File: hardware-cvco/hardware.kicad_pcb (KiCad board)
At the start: 4 copper layers, 99 x 75 mm, 167 parts, among them J1 SMA, J2 SMA, J3 SMA, J4 SMA, J5 SMA, J6 SMA, J7 SMA, J8 Pickit 2, J9 DC, Q1 AOD403, Q2 MBT2222, SW1 On/Off, U1 74LS07, U10 TPS61046, U11 BQ21040, U12 LM324, U13 LM317DCYR, U14 LM386, U2 NLB-310-T1, U3 NLB-310-T1, U4 NLB-310-T1, U5 NLB-310-T1, U6 PIC12F675-ISN, U7 NLB-310-T1, U8 NLB-310-T1, U9 NLB-310-T1, Y1 CVCO55CW-0100-0200, Y2 CVCO55CW-0200-0500, Y3 CV55CW500-1000, Y4 CVCO55CW-1000-2000, Y5 CV55BE1600-3200, Y6 CVCO55CC-3180-3710, Y7 CVCO55CW-3500-4500

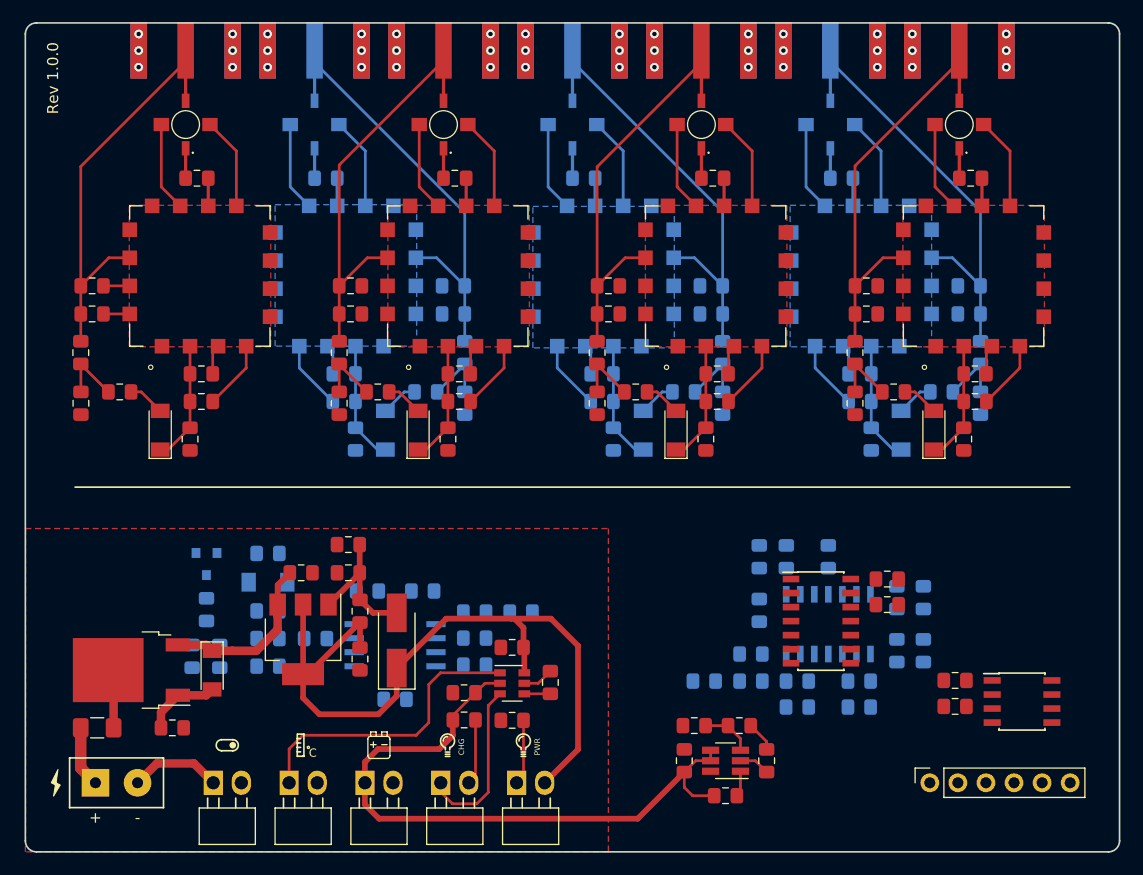
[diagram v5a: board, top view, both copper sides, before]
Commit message: Sweep Generator routing - CVCO.
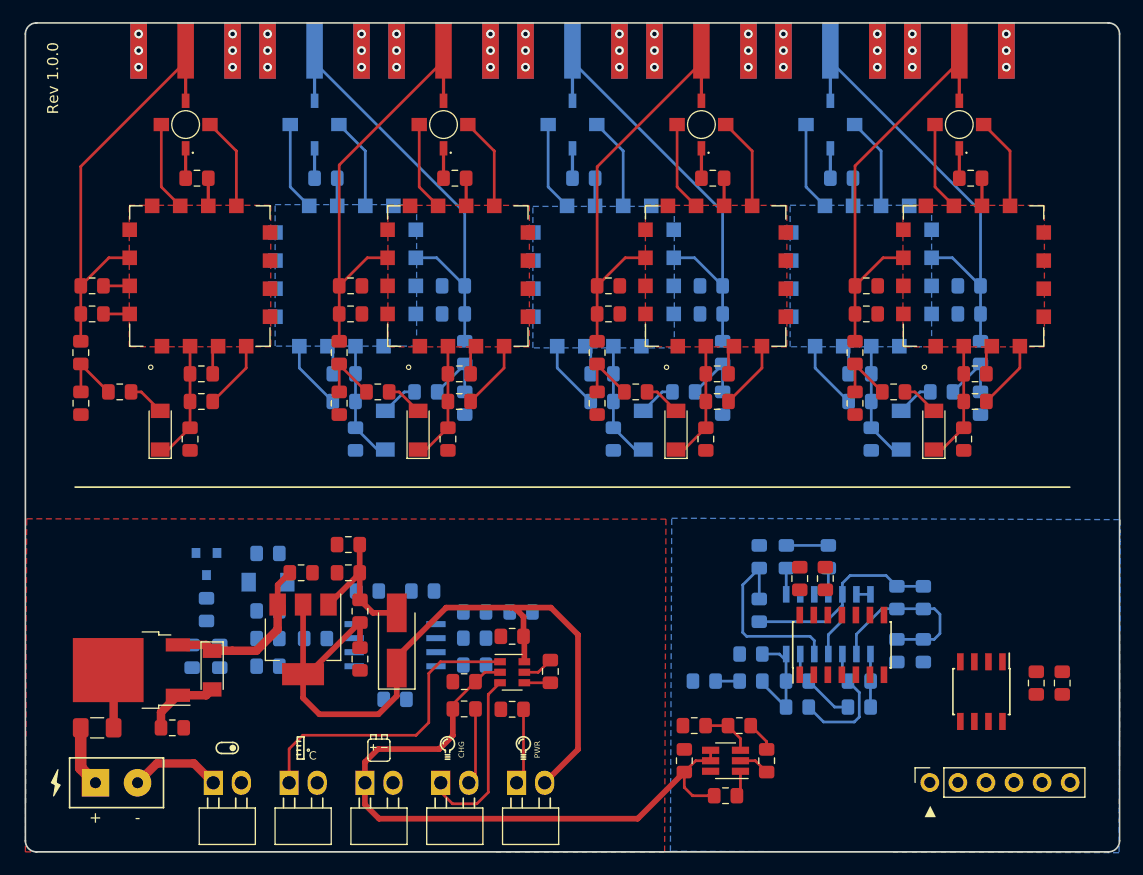
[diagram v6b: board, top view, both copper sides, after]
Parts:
- moved C25 9.92 mm to (159.3, 111.7), turned to 90 degrees
- moved C24 7.92 mm to (135.6, 102.3), turned to 270 degrees
- moved C26 7.35 mm to (157.0, 111.7), turned to 90 degrees
- moved C23 6.08 mm to (137.9, 102.3), turned to 270 degrees
- moved U6 3.78 mm to (152.0, 112.5), turned to 270 degrees
- moved U1 2.87 mm to (139.4, 108.3), turned to 90 degrees
- moved C45 1.00 mm to (105.2, 111.6)
- moved C46 1.00 mm to (109.5, 107.5)
- moved R33 1.00 mm to (105.2, 114.1)
- moved R34 1.00 mm to (113.0, 110.7)
- moved R36 1.00 mm to (109.5, 114.1)
- moved U11 1.00 mm to (109.5, 110.8)
- moved G*** 0.25 mm to (110.6, 117.6)
- moved G*** 0.25 mm to (103.7, 117.6)
- moved G*** 0.25 mm to (90.4, 117.6)
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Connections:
- C23 pad 2: Net-(C23-Pad2) -> P2_VSS
- C24 pad 2: Net-(C23-Pad2) -> P2_VSS
- C25 pad 2: Net-(C25-Pad2) -> P2_VSS
- C26 pad 2: Net-(C25-Pad2) -> P2_VSS
- J8 pad 4: Net-(J8-Pad4) -> GP1
- J8 pad 5: GP1 -> GP0
- J8 pad 6: GP0 -> Net-(J8-Pad6)
- U1 pad 14: Net-(C23-Pad2) -> P2_VDD
- U12 pad 5: Net-(C44-Pad2) -> Net-(R51-Pad1)
- U12 pad 6: Net-(R51-Pad1) -> Net-(C44-Pad2)
- U6 pad 1: Net-(C25-Pad2) -> P2_VDD
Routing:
- net P2_VDD: track 2.75 -> 25.8 mm
- net Net-(R51-Pad1): track 0.00 -> 17.2 mm
- net VGND: track 0.00 -> 16.4 mm
- net Net-(R41-Pad2): track 0.00 -> 11.7 mm
- net Sweep: track 0.00 -> 9.83 mm
- net Net-(C44-Pad2): track 0.00 -> 7.29 mm
- net Net-(R37-Pad2): track 0.00 -> 4.81 mm
- net Net-(R53-Pad2): track 0.00 -> 3.80 mm
- net Tuner: track 0.00 -> 2.38 mm
- net P2_VSS: track 211.3 -> 213.7 mm
- net Net-(C13-Pad1): track 0.00 -> 2.17 mm
- net DC: track 69.2 -> 71.2 mm
- net Net-(U12-Pad13): track 0.00 -> 1.27 mm
- net Net-(D9-Pad2): track 5.93 -> 6.94 mm
- net Net-(TH1-Pad1): track 27.0 -> 28.0 mm
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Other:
- board text added: "▸"

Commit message: Noise Source routing - CVCO.
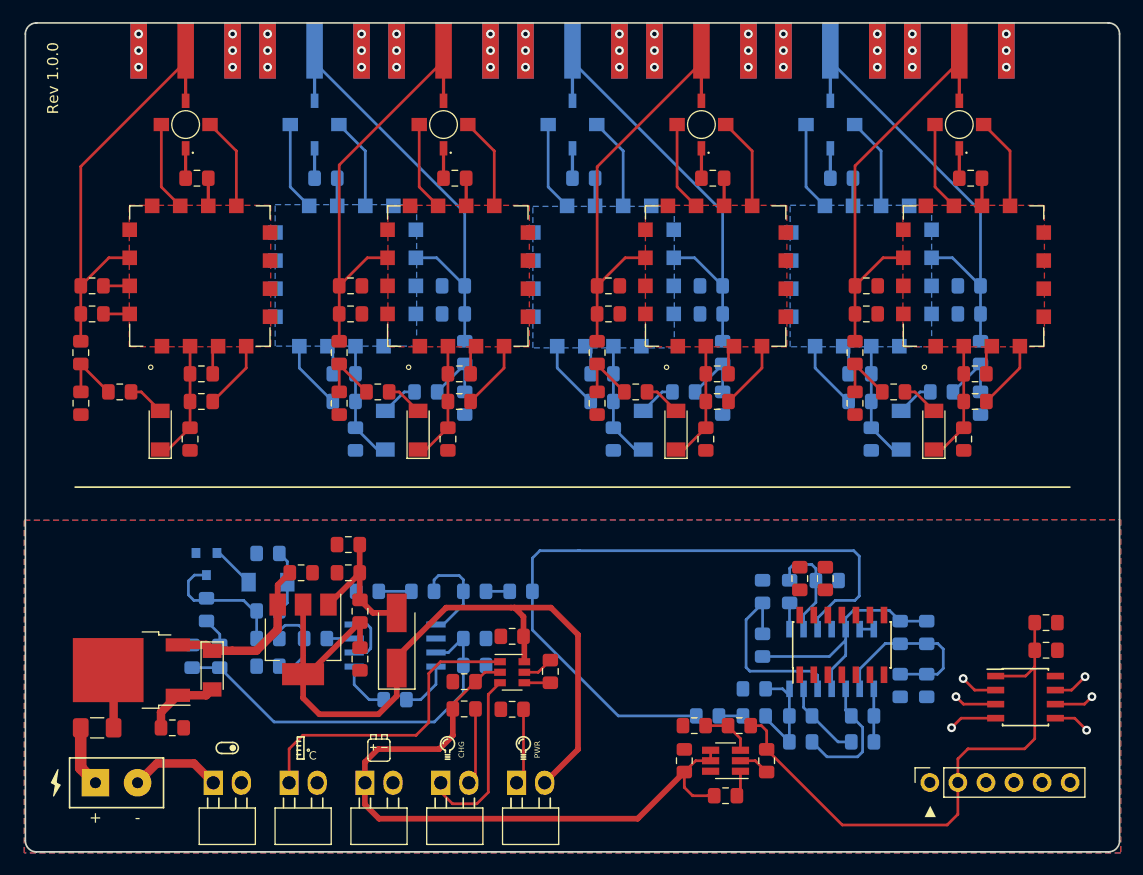
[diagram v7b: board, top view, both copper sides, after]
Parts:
- C47: value 0.1μF -> 1μF
- moved C25 5.66 mm to (157.8, 106.3), turned to 0 degrees
- moved U6 4.02 mm to (156.0, 113.0), turned to 0 degrees
- moved C44 3.16 mm to (135.7, 114.7)
- moved C49 3.16 mm to (144.7, 107.2)
- moved C53 3.16 mm to (144.7, 112.0)
- moved R38 3.16 mm to (147.1, 107.2)
- moved R41 3.16 mm to (141.2, 114.7)
- moved R46 3.16 mm to (147.1, 112.0)
- moved R53 3.16 mm to (134.7, 103.5)
- moved R17 3.16 mm to (127.2, 114.7)
- moved C13 3.16 mm to (131.4, 114.7)
- moved R43 3.16 mm to (131.4, 112.2)
- moved R52 3.16 mm to (132.2, 103.5)
- moved R37 3.16 mm to (141.2, 117.0)
- moved R47 3.16 mm to (135.7, 117.0)
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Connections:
- C47 pad 1: Net-(C47-Pad1) -> P2_VSS
- C48 pad 1: Net-(C47-Pad1) -> P2_VSS
- C56 pad 2: Net-(C50-Pad2) -> Net-(C50-Pad1)
- R45 pad 1: Net-(C50-Pad2) -> Net-(C50-Pad1)
- U14 pad 3: Net-(C50-Pad1) -> Net-(C50-Pad2)
- U14 pad 6: Net-(C47-Pad1) -> Net-(U14-Pad6)
- U14 pad 7: Net-(U14-Pad7) -> Net-(C47-Pad2)
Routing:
- net Net-(R17-Pad1): track 0.00 -> 63.9 mm
- net P2_VDD: track 25.8 -> 76.7 mm
- net Net-(C47-Pad2): track 0.00 -> 35.6 mm
- net GP1: track 0.00 -> 22.6 mm, vias 0 -> 1
- net GP0: track 0.00 -> 15.8 mm, vias 0 -> 1
- net Net-(Q2-Pad3): track 0.00 -> 12.3 mm
- net GP3: track 0.00 -> 10.1 mm, vias 0 -> 1
- net Noise: track 0.00 -> 9.72 mm
- net Net-(C50-Pad1): track 0.00 -> 8.27 mm
- net Net-(R53-Pad2): track 3.80 -> 9.69 mm
- net Net-(C55-Pad2): track 0.00 -> 5.80 mm
- net Net-(C58-Pad2): track 0.00 -> 4.88 mm
- net Net-(C58-Pad1): track 0.00 -> 4.86 mm
- net Net-(D12-Pad2): track 0.00 -> 3.96 mm
- net GP4: track 0.00 -> 3.87 mm, vias 0 -> 1
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
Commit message: PIC routing - CVCO.
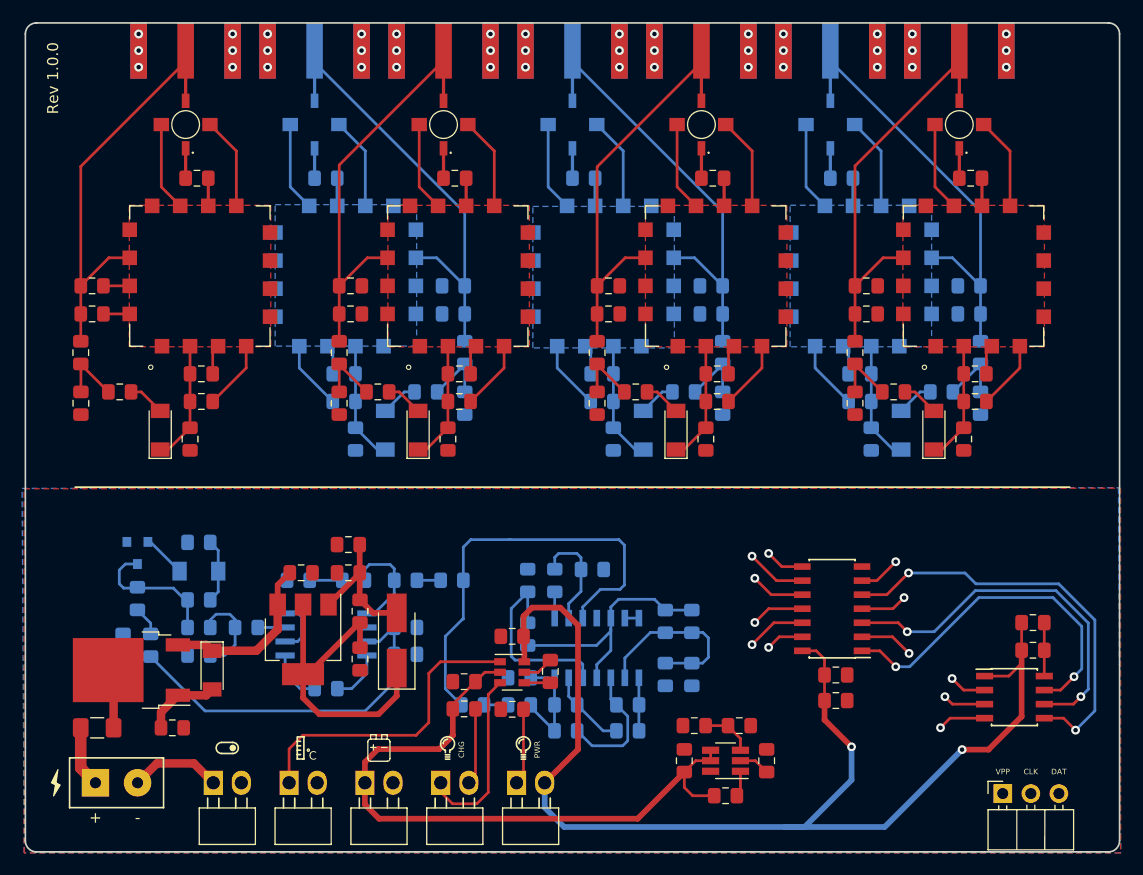
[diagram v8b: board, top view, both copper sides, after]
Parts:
- J8: footprint Connector_PinSocket_2.54mm:PinSocket_1x06_P2.54mm_Vertical -> Connector_PinSocket_2.54mm:PinSocket_1x03_P2.54mm_Horizontal
- moved R38 21.3 mm to (125.8, 106.2)
- moved R46 21.3 mm to (125.8, 111.0)
- moved R54 21.3 mm to (116.8, 101.5)
- moved C44 21.3 mm to (114.4, 113.7)
- moved C49 21.3 mm to (123.4, 106.2)
- moved C53 21.3 mm to (123.4, 111.0)
- moved R17 21.3 mm to (106.0, 113.7)
- moved R37 21.3 mm to (120.0, 116.0)
- moved R41 21.3 mm to (120.0, 113.7)
- moved R47 21.3 mm to (114.4, 116.0)
- moved R53 21.3 mm to (113.4, 102.5)
- moved C13 21.3 mm to (110.2, 113.7)
- moved R43 21.3 mm to (110.2, 111.2)
- moved R51 21.3 mm to (111.0, 107.3)
- moved R52 21.3 mm to (111.0, 102.5)
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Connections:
- BT1 pad 2: P2_VSS -> GND
- C1 pad 2: P2_VSS -> GND
- C14 pad 2: P2_VSS -> GND
- C15 pad 2: P2_VSS -> GND
- C16 pad 2: P2_VSS -> GND
- C17 pad 2: P2_VSS -> GND
- C18 pad 2: P2_VSS -> GND
- C19 pad 2: P2_VSS -> GND
- C2 pad 2: P2_VSS -> GND
- C20 pad 2: P2_VSS -> GND
- C21 pad 2: P2_VSS -> GND
- C23 pad 1: P2_VDD -> VDD
- C23 pad 2: P2_VSS -> GND
- C24 pad 1: P2_VDD -> VDD
- C24 pad 2: P2_VSS -> GND
- C25 pad 1: P2_VDD -> VDD
- C25 pad 2: P2_VSS -> GND
- C26 pad 1: P2_VDD -> VDD
- C26 pad 2: P2_VSS -> GND
- C27 pad 2: P2_VSS -> GND
- C28 pad 2: P2_VSS -> GND
- C29 pad 2: P2_VSS -> GND
- C3 pad 2: P2_VSS -> GND
- C30 pad 2: P2_VSS -> GND
- C31 pad 2: P2_VSS -> GND
- C32 pad 2: P2_VSS -> GND
- C36 pad 1: P2_VDD -> Boost
- C36 pad 2: P2_VSS -> GND
- C37 pad 2: P2_VSS -> GND
- C38 pad 2: P2_VSS -> GND
- C39 pad 2: P2_VSS -> GND
- C4 pad 2: P2_VSS -> GND
- C40 pad 2: P2_VSS -> GND
- C41 pad 2: P2_VSS -> GND
- C42 pad 2: P2_VSS -> GND
- C43 pad 2: P2_VSS -> GND
- C45 pad 2: P2_VSS -> GND
- C46 pad 1: DC -> VDD
- C46 pad 2: P2_VSS -> GND
- C47 pad 1: P2_VSS -> GND
- C48 pad 1: P2_VSS -> GND
- C49 pad 1: P2_VDD -> Boost
- C5 pad 2: P2_VSS -> GND
- C51 pad 2: P2_VSS -> GND
- C52 pad 2: P2_VSS -> GND
- C53 pad 2: P2_VSS -> GND
- C55 pad 1: P2_VSS -> GND
- C56 pad 1: P2_VSS -> GND
- C57 pad 2: P2_VSS -> GND
- C6 pad 2: P2_VSS -> GND
- C7 pad 2: P2_VSS -> GND
- C8 pad 2: P2_VSS -> GND
- D1 pad 2: P2_VSS -> GND
- D2 pad 2: P2_VSS -> GND
- D3 pad 2: P2_VSS -> GND
- D4 pad 2: P2_VSS -> GND
- D5 pad 2: P2_VSS -> GND
- D6 pad 2: P2_VSS -> GND
- D7 pad 2: P2_VSS -> GND
- D8 pad 2: DC -> VDD
- J1 pad 2: P2_VSS -> GND
- J2 pad 2: P2_VSS -> GND
- J3 pad 2: P2_VSS -> GND
- J4 pad 2: P2_VSS -> GND
- J5 pad 2: P2_VSS -> GND
- J6 pad 2: P2_VSS -> GND
- J7 pad 2: P2_VSS -> GND
- J8 pad 2: P2_VDD -> GP0
- J8 pad 3: P2_VSS -> GP1
- Q2 pad 1: P2_VSS -> GND
- R10 pad 2: P2_VSS -> GND
- R11 pad 2: P2_VSS -> GND
- R12 pad 2: P2_VSS -> GND
- R22 pad 2: P2_VDD -> Boost
- R23 pad 2: P2_VDD -> Boost
- R24 pad 2: P2_VDD -> Boost
- R25 pad 2: P2_VSS -> GND
- R26 pad 2: P2_VSS -> GND
- R27 pad 2: P2_VSS -> GND
- R31 pad 1: P2_VDD -> Boost
- R32 pad 2: P2_VSS -> GND
- R34 pad 2: P2_VSS -> GND
- R35 pad 2: P2_VDD -> Boost
- R36 pad 2: P2_VSS -> GND
- R38 pad 2: P2_VDD -> Boost
- R39 pad 1: P2_VDD -> Boost
- R40 pad 2: P2_VSS -> GND
- R43 pad 1: P2_VSS -> GND
- R46 pad 1: P2_VSS -> GND
- R48 pad 2: P2_VSS -> GND
- R49 pad 2: P2_VSS -> GND
- R5 pad 2: P2_VDD -> Boost
- R50 pad 2: P2_VSS -> GND
- R51 pad 2: P2_VDD -> Boost
- R52 pad 1: P2_VSS -> GND
- R54 pad 2: P2_VSS -> GND
- R6 pad 2: P2_VDD -> Boost
- R7 pad 2: P2_VDD -> Boost
- R8 pad 2: P2_VDD -> Boost
- R9 pad 2: P2_VSS -> GND
- SW1 pad 2: P2_VSS -> GND
- TH1 pad 2: P2_VSS -> GND
- U1 pad 10: P2_VDD -> Boost
- U1 pad 12: P2_VDD -> Boost
- U1 pad 14: P2_VDD -> VDD
- U1 pad 2: P2_VDD -> Boost
- U1 pad 4: P2_VDD -> Boost
- U1 pad 6: P2_VDD -> Boost
- U1 pad 7: P2_VSS -> GND
- U1 pad 8: P2_VDD -> Boost
- U10 pad 2: P2_VSS -> GND
- U11 pad 5: P2_VSS -> GND
- U11 pad 6: DC -> VDD
- U12 pad 11: P2_VSS -> GND
- U12 pad 12: P2_VDD -> Boost
- U12 pad 4: P2_VDD -> Boost
- U14 pad 2: P2_VSS -> GND
- U14 pad 4: P2_VSS -> GND
- U2 pad 2: P2_VSS -> GND
- U2 pad 4: P2_VSS -> GND
- U3 pad 2: P2_VSS -> GND
- U3 pad 4: P2_VSS -> GND
- U4 pad 2: P2_VSS -> GND
- U4 pad 4: P2_VSS -> GND
- U5 pad 2: P2_VSS -> GND
- U5 pad 4: P2_VSS -> GND
- U6 pad 1: P2_VDD -> VDD
- U6 pad 8: P2_VSS -> GND
- U7 pad 2: P2_VSS -> GND
- U7 pad 4: P2_VSS -> GND
- U8 pad 2: P2_VSS -> GND
- U8 pad 4: P2_VSS -> GND
- U9 pad 2: P2_VSS -> GND
- U9 pad 4: P2_VSS -> GND
- Y1 pad 1: P2_VSS -> GND
- Y1 pad 11: P2_VSS -> GND
- Y1 pad 12: P2_VSS -> GND
- Y1 pad 13: P2_VSS -> GND
- Y1 pad 15: P2_VSS -> GND
- Y1 pad 16: P2_VSS -> GND
- Y1 pad 3: P2_VSS -> GND
- Y1 pad 4: P2_VSS -> GND
- Y1 pad 5: P2_VSS -> GND
- Y1 pad 6: P2_VSS -> GND
- Y1 pad 7: P2_VSS -> GND
- Y1 pad 8: P2_VSS -> GND
- Y1 pad 9: P2_VSS -> GND
- Y2 pad 1: P2_VSS -> GND
- Y2 pad 11: P2_VSS -> GND
- Y2 pad 12: P2_VSS -> GND
- Y2 pad 13: P2_VSS -> GND
- Y2 pad 15: P2_VSS -> GND
- Y2 pad 16: P2_VSS -> GND
- Y2 pad 3: P2_VSS -> GND
- Y2 pad 4: P2_VSS -> GND
- Y2 pad 5: P2_VSS -> GND
- Y2 pad 6: P2_VSS -> GND
- Y2 pad 7: P2_VSS -> GND
- Y2 pad 8: P2_VSS -> GND
- Y2 pad 9: P2_VSS -> GND
- Y3 pad 1: P2_VSS -> GND
- Y3 pad 11: P2_VSS -> GND
- Y3 pad 12: P2_VSS -> GND
- Y3 pad 13: P2_VSS -> GND
- Y3 pad 15: P2_VSS -> GND
- Y3 pad 16: P2_VSS -> GND
- Y3 pad 3: P2_VSS -> GND
- Y3 pad 4: P2_VSS -> GND
- Y3 pad 5: P2_VSS -> GND
- Y3 pad 6: P2_VSS -> GND
- Y3 pad 7: P2_VSS -> GND
- Y3 pad 8: P2_VSS -> GND
- Y3 pad 9: P2_VSS -> GND
- Y4 pad 1: P2_VSS -> GND
- Y4 pad 11: P2_VSS -> GND
- Y4 pad 12: P2_VSS -> GND
- Y4 pad 13: P2_VSS -> GND
- Y4 pad 15: P2_VSS -> GND
- Y4 pad 16: P2_VSS -> GND
- Y4 pad 3: P2_VSS -> GND
- Y4 pad 4: P2_VSS -> GND
- Y4 pad 5: P2_VSS -> GND
- Y4 pad 6: P2_VSS -> GND
- Y4 pad 7: P2_VSS -> GND
- Y4 pad 8: P2_VSS -> GND
- Y4 pad 9: P2_VSS -> GND
- Y5 pad 1: P2_VSS -> GND
- Y5 pad 11: P2_VSS -> GND
- Y5 pad 12: P2_VSS -> GND
- Y5 pad 13: P2_VSS -> GND
- Y5 pad 15: P2_VSS -> GND
- Y5 pad 16: P2_VSS -> GND
- Y5 pad 3: P2_VSS -> GND
- Y5 pad 4: P2_VSS -> GND
- Y5 pad 5: P2_VSS -> GND
- Y5 pad 6: P2_VSS -> GND
- Y5 pad 7: P2_VSS -> GND
- Y5 pad 8: P2_VSS -> GND
- Y5 pad 9: P2_VSS -> GND
- Y6 pad 1: P2_VSS -> GND
- Y6 pad 11: P2_VSS -> GND
- Y6 pad 12: P2_VSS -> GND
- Y6 pad 13: P2_VSS -> GND
- Y6 pad 15: P2_VSS -> GND
- Y6 pad 16: P2_VSS -> GND
- Y6 pad 3: P2_VSS -> GND
- Y6 pad 4: P2_VSS -> GND
- Y6 pad 5: P2_VSS -> GND
- Y6 pad 6: P2_VSS -> GND
- Y6 pad 7: P2_VSS -> GND
- Y6 pad 8: P2_VSS -> GND
- Y6 pad 9: P2_VSS -> GND
- Y7 pad 1: P2_VSS -> GND
- Y7 pad 11: P2_VSS -> GND
- Y7 pad 12: P2_VSS -> GND
- Y7 pad 13: P2_VSS -> GND
- Y7 pad 15: P2_VSS -> GND
- Y7 pad 16: P2_VSS -> GND
- Y7 pad 3: P2_VSS -> GND
- Y7 pad 4: P2_VSS -> GND
- Y7 pad 5: P2_VSS -> GND
- Y7 pad 6: P2_VSS -> GND
- Y7 pad 7: P2_VSS -> GND
- Y7 pad 8: P2_VSS -> GND
- Y7 pad 9: P2_VSS -> GND
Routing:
- net GND: track 0.00 -> 221.3 mm, vias 0 -> 42
- net P2_VSS: track 216.5 -> 0.00 mm, vias 42 -> 0
- net VDD: track 0.00 -> 111.3 mm, vias 0 -> 2
- net P2_VDD: track 76.7 -> 0.00 mm
- net Boost: track 0.00 -> 52.5 mm, vias 0 -> 6
- net DC: track 71.2 -> 32.0 mm
- net GP2: track 3.28 -> 37.6 mm, vias 1 -> 2
- net GP0: track 15.8 -> 45.8 mm, vias 1 -> 2
- net Net-(R17-Pad1): track 63.9 -> 39.8 mm
- net GP1: track 22.6 -> 46.2 mm, vias 1 -> 2
- net GP3: track 10.1 -> 20.1 mm, vias 1 -> 2
- net GP4: track 3.87 -> 8.69 mm, vias 1 -> 2
- net GP5: track 3.37 -> 6.82 mm, vias 1 -> 2
- added copper zone on B.Cu, net GND
- added copper zone on F.Cu, net GND
- added copper zone on In1.Cu, net GND
- added copper zone on In2.Cu, net GND
- removed copper zone on B.Cu, net P2_VSS
- removed copper zone on F.Cu, net P2_VSS
- removed copper zone on In1.Cu, net P2_VSS
- removed copper zone on In2.Cu, net P2_VSS
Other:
- board text added: "CLK"
- board text added: "DAT"
- board text added: "VPP"
- board text removed: "▸"
